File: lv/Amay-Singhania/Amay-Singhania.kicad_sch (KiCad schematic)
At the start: 34 parts, among them IC1 TLV4888DR, SW5 SW_DIP_x04, SW6 SW_DIP_x02, U5 ADS122C14IRTER

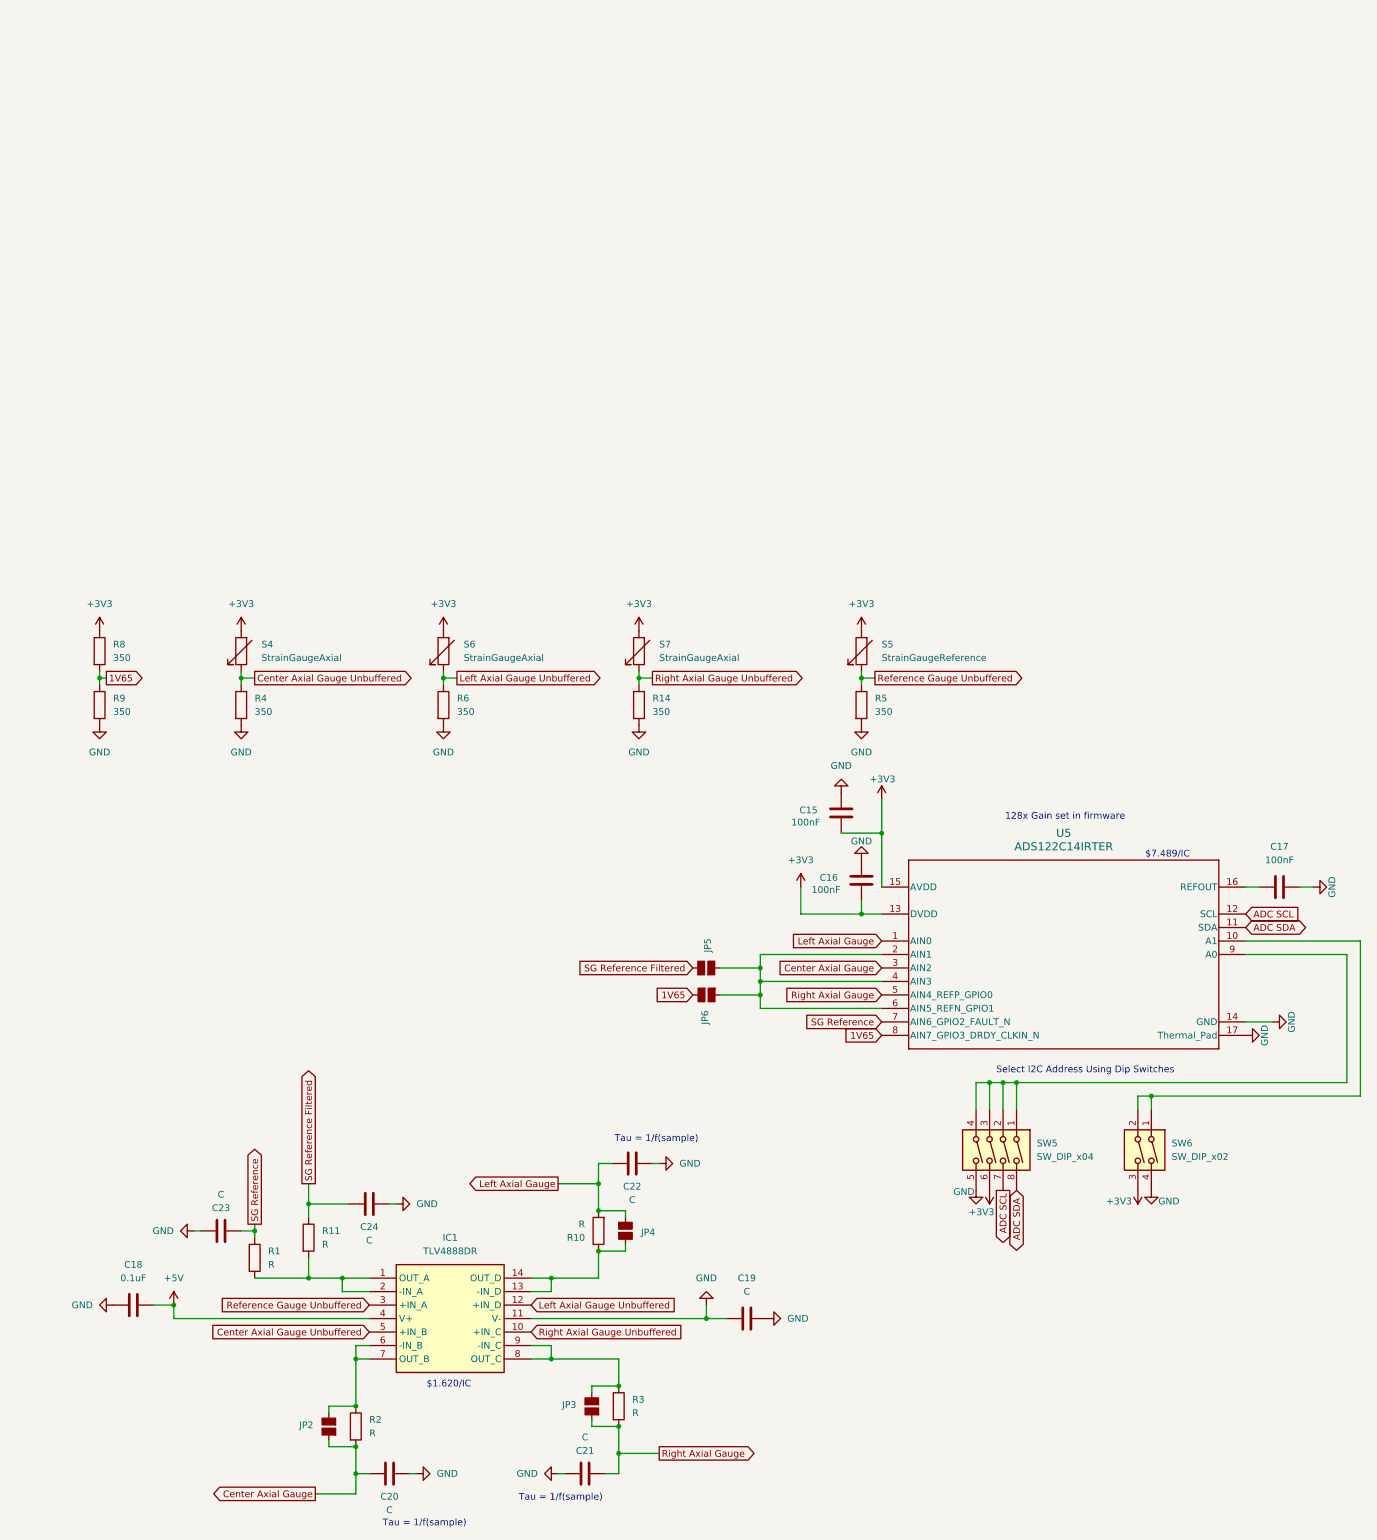
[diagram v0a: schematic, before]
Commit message: Updated PCB with RC values for low pass filter. has old onboarding sheets with in-Amp and other designs, will be removed in next commit
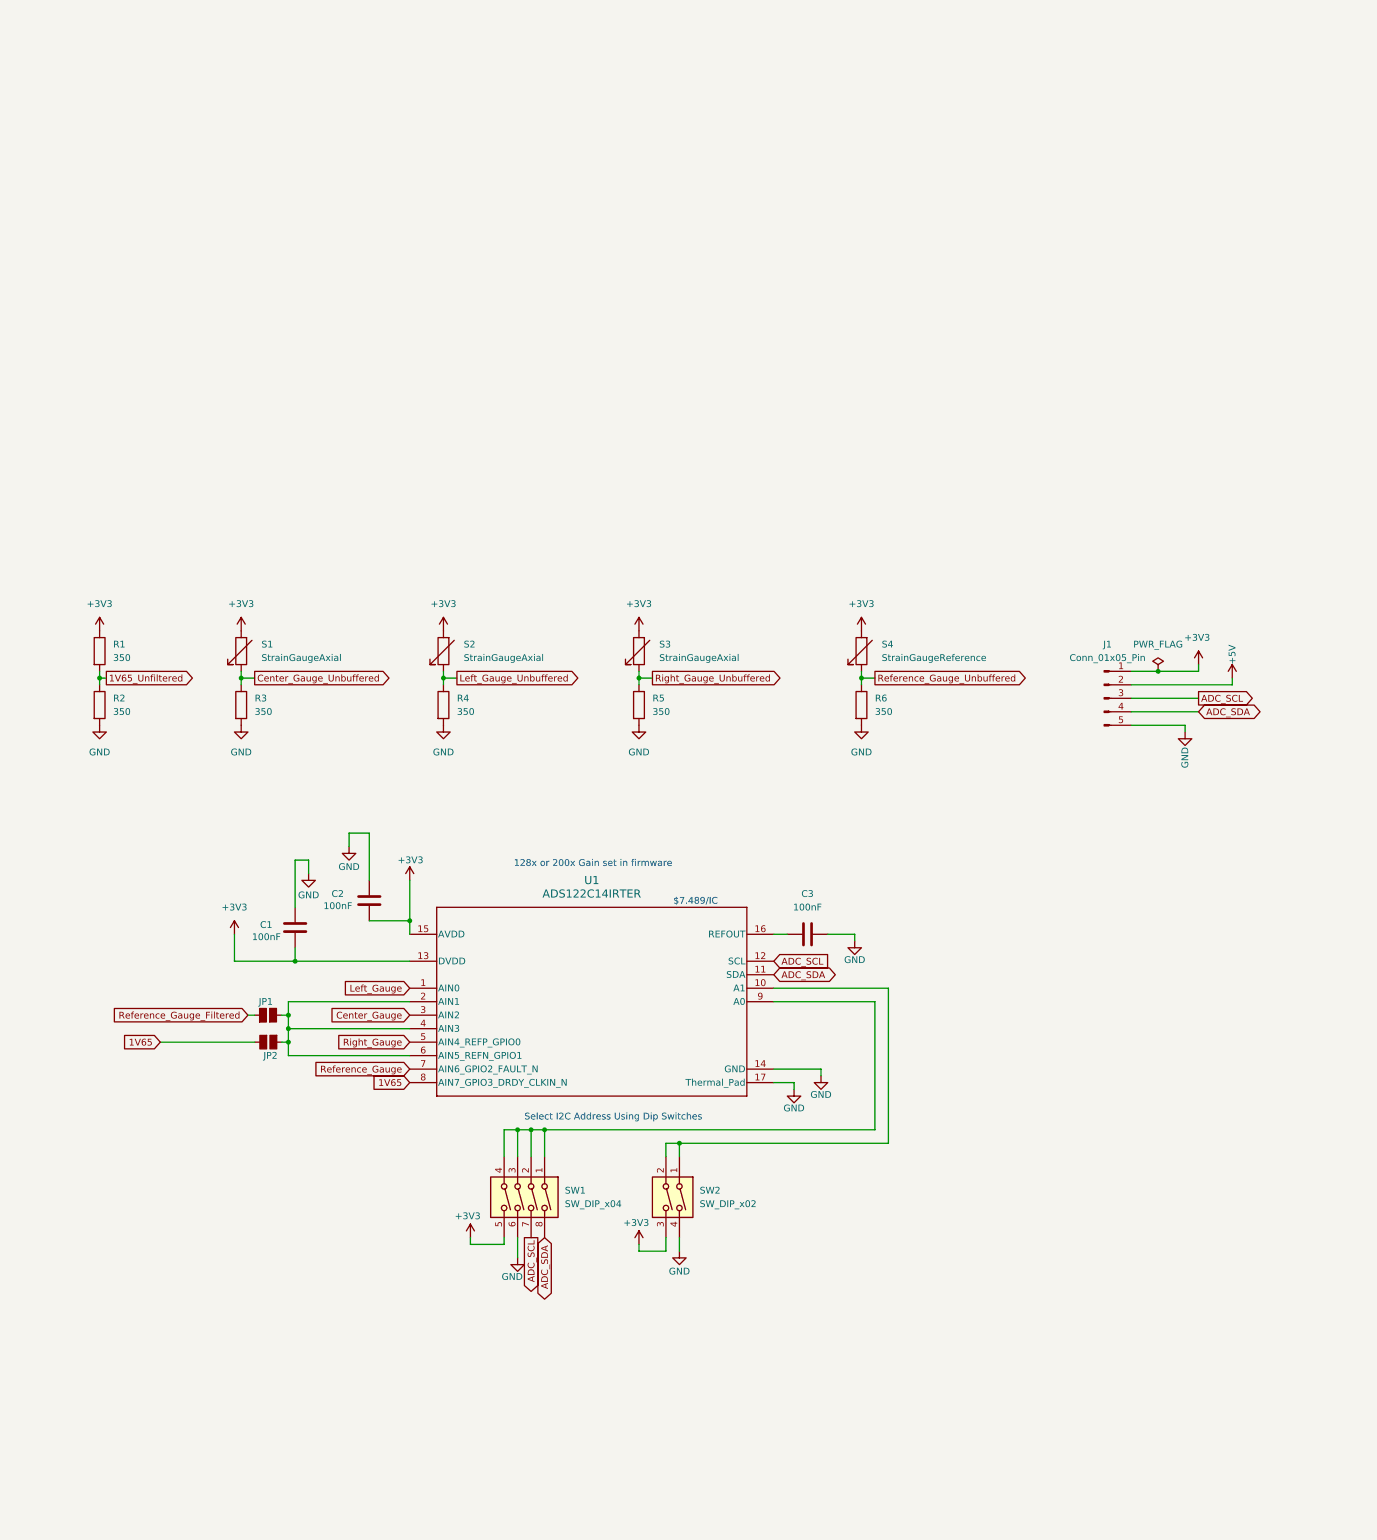
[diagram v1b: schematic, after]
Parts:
- removed C18: 0.1uF, Package_TO_SOT_SMD:TSOT-23-5, symbol Device:C
- removed C19, C20, C21, C22, C23, C24: C, Package_TO_SOT_SMD:TSOT-23-5, symbol Device:C
- removed IC1: TLV4888DR, SOIC127P600X175-14N, symbol TLV4888DR:TLV4888DR
- removed JP2, JP3, JP4: (no value), Package_TO_SOT_SMD:SOT-23-6_Handsoldering, symbol formula_slug_symbol_library:SolderJumper_Open_Small
- removed R1, R10, R11, R2, R3: R, Package_DIP:DIP-8_W7.62mm, symbol Device:R
- added J1: Conn_01x05_Pin, symbol Connector:Conn_01x05_Pin
- C1: renamed from C16; footprint Package_TO_SOT_SMD:TSOT-23-5 -> Capacitor_SMD:C_0402_1005Metric
- C2: renamed from C15; footprint Package_TO_SOT_SMD:TSOT-23-5 -> Capacitor_SMD:C_0402_1005Metric
- C3: renamed from C17; footprint Package_TO_SOT_SMD:TSOT-23-5 -> Capacitor_SMD:C_0402_1005Metric
- JP1: renamed from JP5; footprint Package_TO_SOT_SMD:SOT-23-6_Handsoldering -> Jumper:SolderJumper-2_P1.3mm_Open_Pad1.0x1.5mm
- JP2: renamed from JP6; footprint Package_TO_SOT_SMD:SOT-23-6_Handsoldering -> Jumper:SolderJumper-2_P1.3mm_Open_Pad1.0x1.5mm
- R1: renamed from R8; footprint Resistor_SMD:R_01005_0402Metric -> Resistor_SMD:R_0402_1005Metric
- R2: renamed from R9; footprint Resistor_SMD:R_01005_0402Metric -> Resistor_SMD:R_0402_1005Metric
- R3: renamed from R4; footprint Resistor_SMD:R_01005_0402Metric -> Resistor_SMD:R_0402_1005Metric
- R4: renamed from R6; footprint Resistor_SMD:R_01005_0402Metric -> Resistor_SMD:R_0402_1005Metric
- R5: renamed from R14; footprint Resistor_SMD:R_01005_0402Metric -> Resistor_SMD:R_0402_1005Metric
- R6: renamed from R5; footprint Resistor_SMD:R_01005_0402Metric -> Resistor_SMD:R_0402_1005Metric
- SW1: renamed from SW5; footprint (none) -> Button_Switch_SMD:SW_DIP_SPSTx04_Slide_6.7x11.72mm_W6.73mm_P2.54mm_LowProfile_JPin
- SW2: renamed from SW6; footprint (none) -> Button_Switch_SMD:SW_DIP_SPSTx02_Slide_6.7x6.64mm_W6.73mm_P2.54mm_LowProfile_JPin
- renumbered S4 to S1, S6 to S2, S7 to S3, S5 to S4, U5 to U1
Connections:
- net +3V3: now also SW1.5, J1.1 (Pin_1); no longer SW1.6
- net +5V: now also J1.2 (Pin_2)
- net 1V65: no longer R1.2, R2.1
- net GND: now also SW1.6, J1.5 (Pin_5); no longer SW1.5
- net ADC SCL renamed ADC_SCL
- net ADC_SCL: now also J1.3 (Pin_3)
- net ADC SDA renamed ADC_SDA
- net ADC_SDA: now also J1.4 (Pin_4)
- net Center Axial Gauge renamed Center_Gauge
- net Center Axial Gauge Unbuffered renamed Center_Gauge_Unbuffered
- net Left Axial Gauge renamed Left_Gauge
- net Left Axial Gauge Unbuffered renamed Left_Gauge_Unbuffered
- net Reference Gauge Unbuffered renamed Reference_Gauge_Unbuffered
- net Right Axial Gauge renamed Right_Gauge
- net Right Axial Gauge Unbuffered renamed Right_Gauge_Unbuffered
- net SG Reference renamed Reference_Gauge
- net SG Reference Filtered renamed Reference_Gauge_Filtered
- new net 1V65_Unfiltered: R1.2, R2.1
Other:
- note added: "128x or 200x Gain set in firmware"
- note removed: "$1.620/IC"
- note removed: "128x Gain set in firmware"
- note removed: "Tau = 1/f(sample)"
- moved on the sheet: C1, C2, C3, JP1, JP2, SW1, SW2, U1

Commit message: remove old schematic files; renamed and moved some things
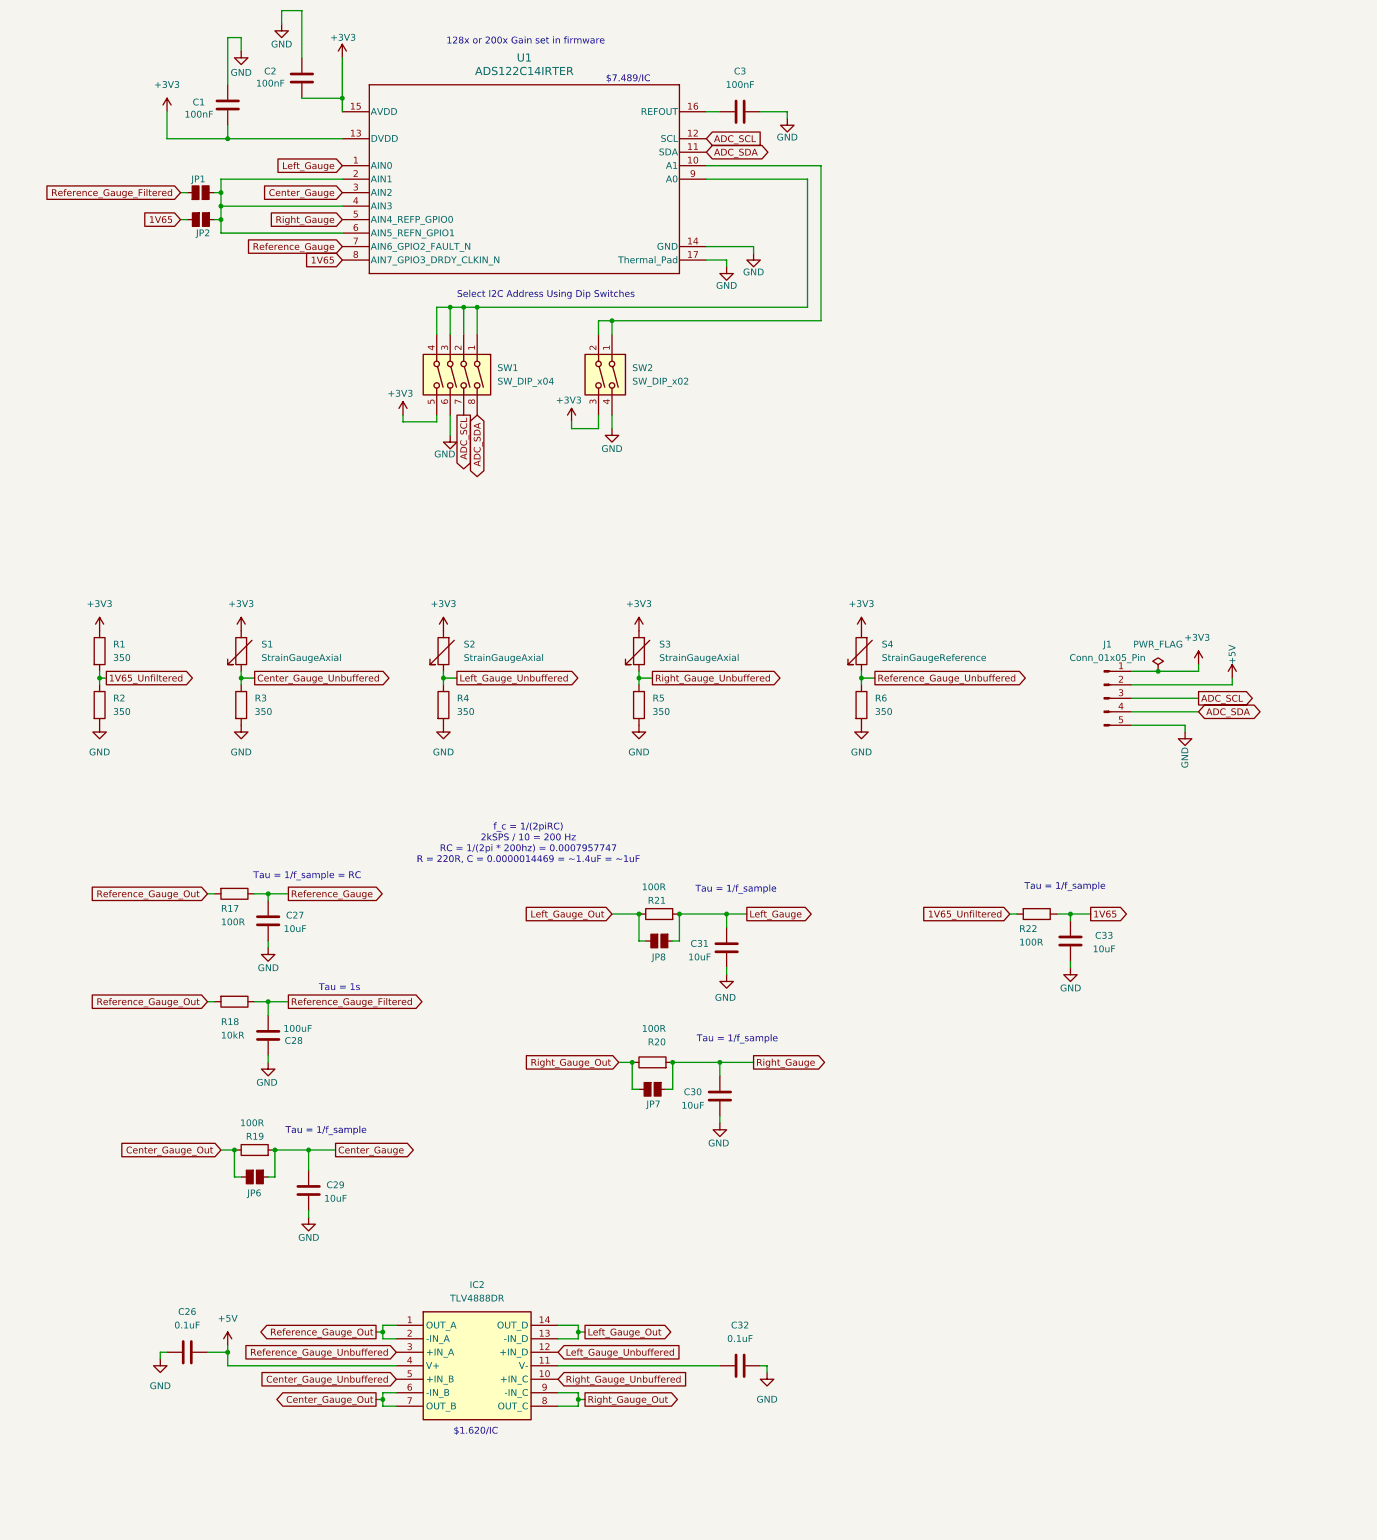
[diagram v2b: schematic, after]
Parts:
- added C26, C32: 0.1uF, Capacitor_SMD:C_0402_1005Metric, symbol Device:C
- added C27, C29, C30, C31, C33: 10uF, Capacitor_SMD:C_0402_1005Metric, symbol Device:C
- added C28: 100uF, Capacitor_SMD:C_0402_1005Metric, symbol Device:C
- added IC2: TLV4888DR, TLV4888DR:SOIC127P600X175-14N, symbol TLV4888DR:TLV4888DR
- added JP6, JP7, JP8: (no value), Jumper:SolderJumper-2_P1.3mm_Open_Pad1.0x1.5mm, symbol formula_slug_symbol_library:SolderJumper_Open_Small
- added R17, R19, R20, R21, R22: 100R, Resistor_SMD:R_0402_1005Metric, symbol Device:R
- added R18: 10kR, Resistor_SMD:R_0402_1005Metric, symbol Device:R
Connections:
- net +5V: now also C26.1, IC2.4 (V+)
- net 1V65: now also C33.2, R22.1
- net 1V65_Unfiltered: now also R22.2
- net Center_Gauge: now also C29.2, JP6.1, R19.2
- net Center_Gauge_Unbuffered: now also IC2.5 (+IN_B)
- net GND: now also C26.2, C27.1, C28.1, C29.1, C30.1, C31.1, C32.2, C33.1
- net Left_Gauge: now also C31.2, JP8.1, R21.2
- net Left_Gauge_Unbuffered: now also IC2.12 (+IN_D)
- net Reference_Gauge: now also C27.2, R17.1
- net Reference_Gauge_Filtered: now also C28.2, R18.1
- net Reference_Gauge_Unbuffered: now also IC2.3 (+IN_A)
- net Right_Gauge: now also C30.2, JP7.1, R20.2
- net Right_Gauge_Unbuffered: now also IC2.10 (+IN_C)
- new net: C32.1, IC2.11 (V-)
- new net Center_Gauge_Out: IC2.6 (-IN_B), IC2.7 (OUT_B), JP6.2, R19.1
- new net Left_Gauge_Out: IC2.13 (-IN_D), IC2.14 (OUT_D), JP8.2, R21.1
- new net Reference_Gauge_Out: IC2.1 (OUT_A), IC2.2 (-IN_A), R17.2, R18.2
- new net Right_Gauge_Out: IC2.8 (OUT_C), IC2.9 (-IN_C), JP7.2, R20.1
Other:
- note added: "$1.620/IC"
- note added: "Tau = 1/f_sample"
- note added: "Tau = 1/f_sample = RC"
- note added: "Tau = 1s"
- note added: "f_c = 1/(2piRC) 2kSPS / 10 = 200 Hz RC = 1/(2pi * 200hz) = 0.0007957747 R = 220R, C = 0.0000014469 = ~1.4uF = ~1uF"
- moved on the sheet: C1, C2, C3, JP1, JP2, SW1, SW2, U1

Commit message: wjker
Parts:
- removed C1, C2, C3: 100nF, Capacitor_SMD:C_0402_1005Metric, symbol Device:C
- removed J1: Conn_01x05_Pin, symbol Connector:Conn_01x05_Pin
- removed JP1, JP2: (no value), Jumper:SolderJumper-2_P1.3mm_Open_Pad1.0x1.5mm, symbol formula_slug_symbol_library:SolderJumper_Open_Small
- removed SW1: SW_DIP_x04, Button_Switch_SMD:SW_DIP_SPSTx04_Slide_6.7x11.72mm_W6.73mm_P2.54mm_LowProfile_JPin, symbol Switch:SW_DIP_x04
- removed SW2: SW_DIP_x02, Button_Switch_SMD:SW_DIP_SPSTx02_Slide_6.7x6.64mm_W6.73mm_P2.54mm_LowProfile_JPin, symbol Switch:SW_DIP_x02
- removed U1: ADS122C14IRTER, RTE0016C-IPC_A, symbol ADS122C14:ADS122C14IRTER
- added J1: Conn_01x05, Package_DFN_QFN:QFN-20-1EP_5x5mm_P0.65mm_EP3.35x3.35mm, symbol Connector_Generic:Conn_01x05
- added R13, R14: 4.7kR, Resistor_SMD:R_0402_1005Metric, symbol Device:R
- C2: renamed from C27; value 10uF -> 0.1uF
- C4: renamed from C29; value 10uF -> 0.1uF
- C5: renamed from C33; value 10uF -> 0.1uF
- C6: renamed from C30; value 10uF -> 0.1uF
- C7: renamed from C31; value 10uF -> 0.1uF
- R10: renamed from R21; value 100R -> 470R
- R11: renamed from R22; value 100R -> 470R
- R3: renamed from R17; value 100R -> 470R
- R6: renamed from R19; value 100R -> 470R
- R9: renamed from R20; value 100R -> 470R
- renumbered C26 to C1, C28 to C3, C32 to C8, IC2 to IC1, JP6 to JP1, JP7 to JP2, JP8 to JP3, R6 to R12, R18 to R4, R3 to R5, R4 to R7, R5 to R8
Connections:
- net +3V3: now also J1.1 (Pin_1), R13.1, R14.1
- net +5V: now also J1.2 (Pin_2)
- net ADC_SCL: now also J1.3 (Pin_3), R13.2
- net ADC_SDA: now also J1.4 (Pin_4), R14.2
- net GND: now also J1.5 (Pin_5)
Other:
- note added: "Tau = 1/f_sample = 1/20kHz = 0.00005 RC = 0.00005 R = 470R C = 0.0005/470 = 0.0000001064 = ~0.1uF"
- note removed: "$7.489/IC"
- note removed: "128x or 200x Gain set in firmware"
- note removed: "Select I2C Address Using Dip Switches"
- note removed: "Tau = 1/f_sample = RC"
- note removed: "f_c = 1/(2piRC) 2kSPS / 10 = 200 Hz RC = 1/(2pi * 200hz) = 0.0007957747 R = 220R, C = 0.0000014469 = ~1.4uF = ~1uF"
- moved on the sheet: C4, C5, JP1, R11, R6
